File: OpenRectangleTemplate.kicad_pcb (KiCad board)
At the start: 2 copper layers, 38.1 x 49.2 mm, 40 parts, among them J1 USB C Connector, J2 JTAG_TC2030, SW1 Boot, U1 XC6206, U2 USBLC6-2SC6, U3 RP2040, U4 W25Q128JVS, Y1 12MHz

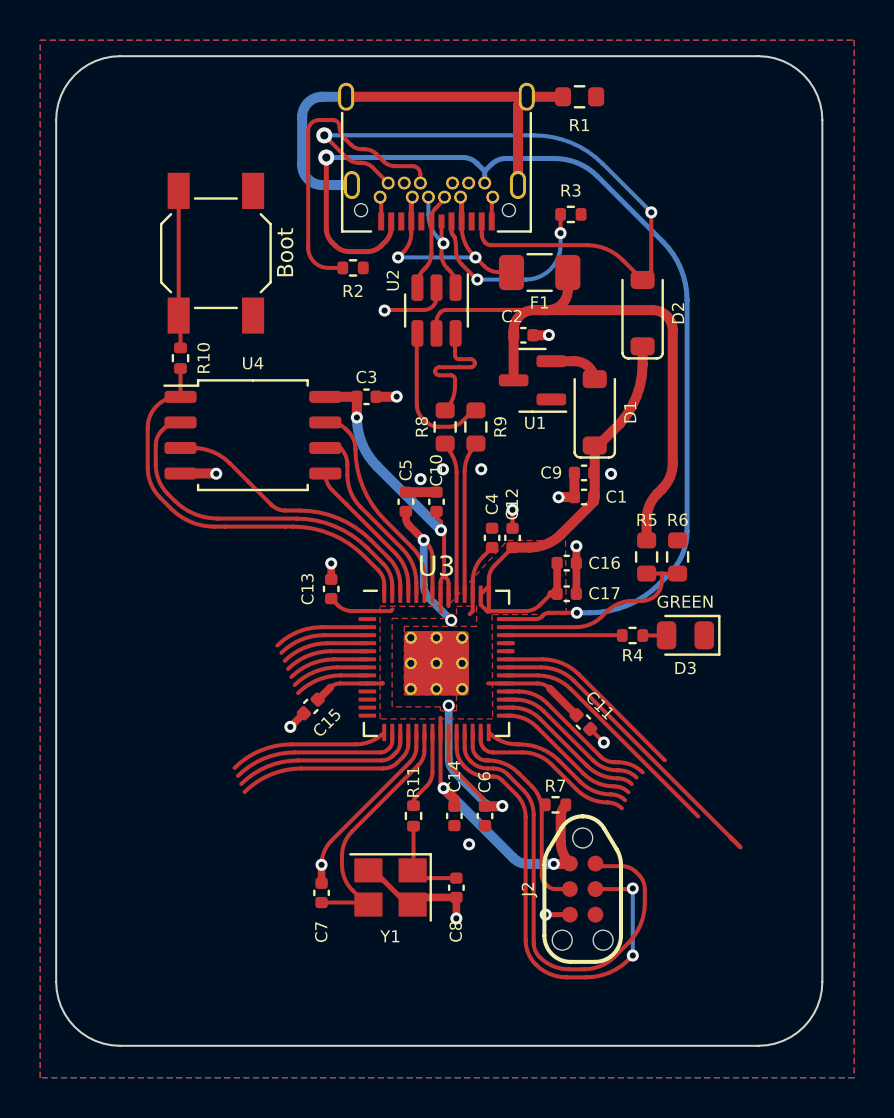
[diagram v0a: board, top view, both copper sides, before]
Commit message: Reverted back to pico pinout
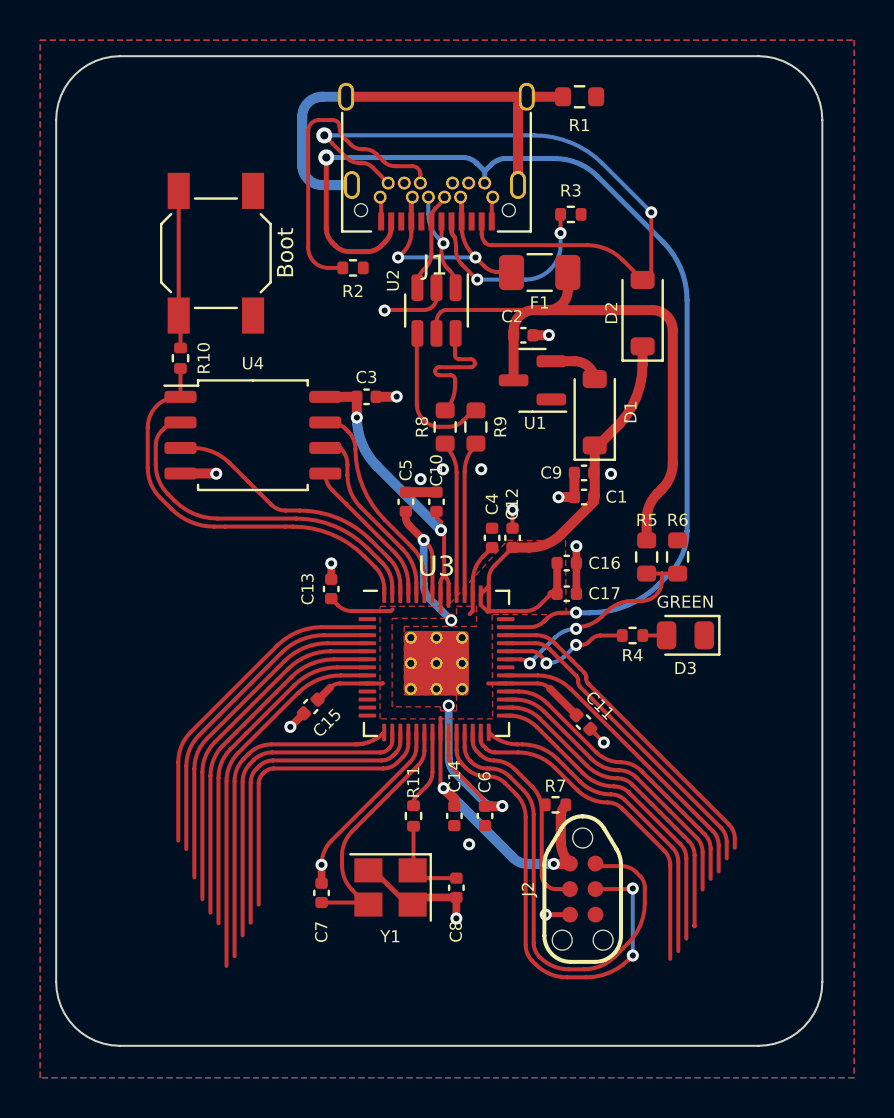
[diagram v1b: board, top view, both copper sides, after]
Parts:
- D1, D2: footprint qw-footprints:CUSTOM D_SOD-123 -> Diode_SMD:D_SOD-123
- J1: footprint qw-footprints:TYPE-C_24P_QCHT -> footprints:TYPE-C_24P_QCHT
- U3: footprint qw-footprints:RP2040-QFN-56 -> footprints:RP2040-QFN-56
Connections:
- U3 pad 15: C_LT -> C_UP
- U3 pad 16: A -> C_LT
- U3 pad 17: C_DN -> A
- U3 pad 18: C_RT -> C_DN
- U3 pad 27: C_UP -> C_RT
- U3 pad 35: B -> unconnected-(U3-GPIO23-Pad35)
- U3 pad 36: R -> VBUS_SENSE
- U3 pad 37: unconnected-(U3-GPIO25-Pad37) -> PICO_LED
- U3 pad 38: unconnected-(U3-GPIO26/ADC0-Pad38) -> B
- U3 pad 39: PICO_LED -> R
- U3 pad 40: VBUS_SENSE -> DATA
- U3 pad 41: DATA -> unconnected-(U3-GPIO29/ADC3-Pad41)
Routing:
- net M2: track 3.67 -> 18.6 mm
- net M1: track 3.83 -> 17.2 mm
- net L: track 4.00 -> 17.3 mm
- net LEFT: track 4.16 -> 17.3 mm
- net DOWN: track 4.33 -> 16.9 mm
- net START: track 4.70 -> 16.3 mm
- net RIGHT: track 4.50 -> 16.1 mm
- net C_LT: track 7.88 -> 16.5 mm
- net C_UP: track 8.65 -> 17.3 mm
- net UP: track 7.80 -> 16.4 mm
- net MS: track 7.45 -> 15.9 mm
- net Z: track 7.61 -> 15.9 mm
- net C_RT: track 9.64 -> 17.0 mm
- net A: track 8.64 -> 16.0 mm
- net LS: track 7.88 -> 14.8 mm
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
